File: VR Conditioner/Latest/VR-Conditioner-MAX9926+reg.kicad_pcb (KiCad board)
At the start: 2 copper layers, 19.7 x 19.7 mm, 22 parts, among them J1 8-pin header, J2 Edge, U1 MAX9926UAEE+, U2 AMS1117CD-5.0

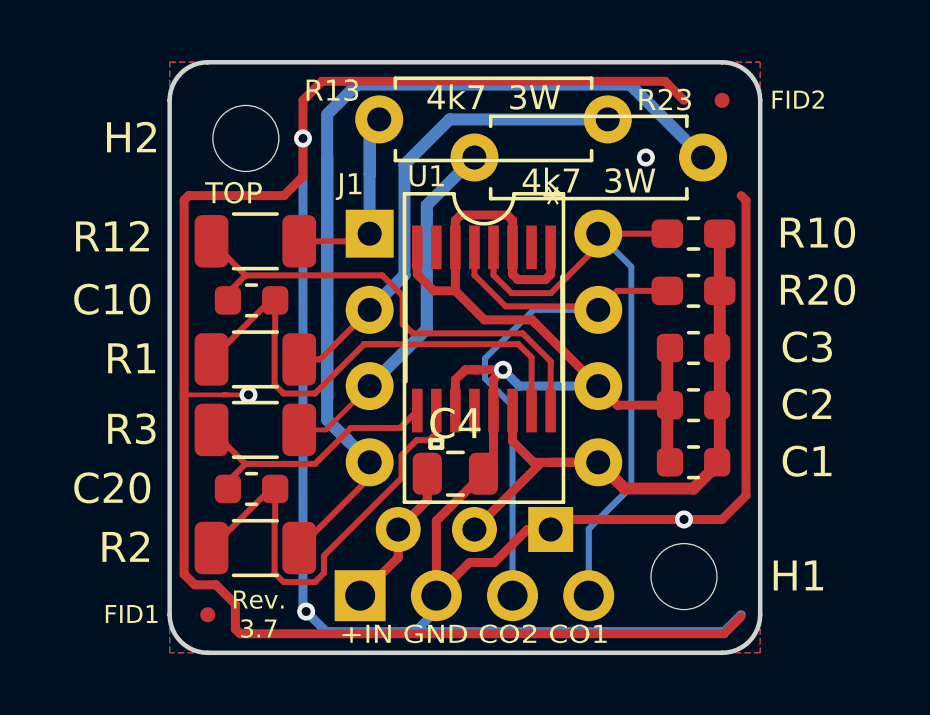
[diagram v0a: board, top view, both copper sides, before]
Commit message: Add prod files for MAX9926 VR cond
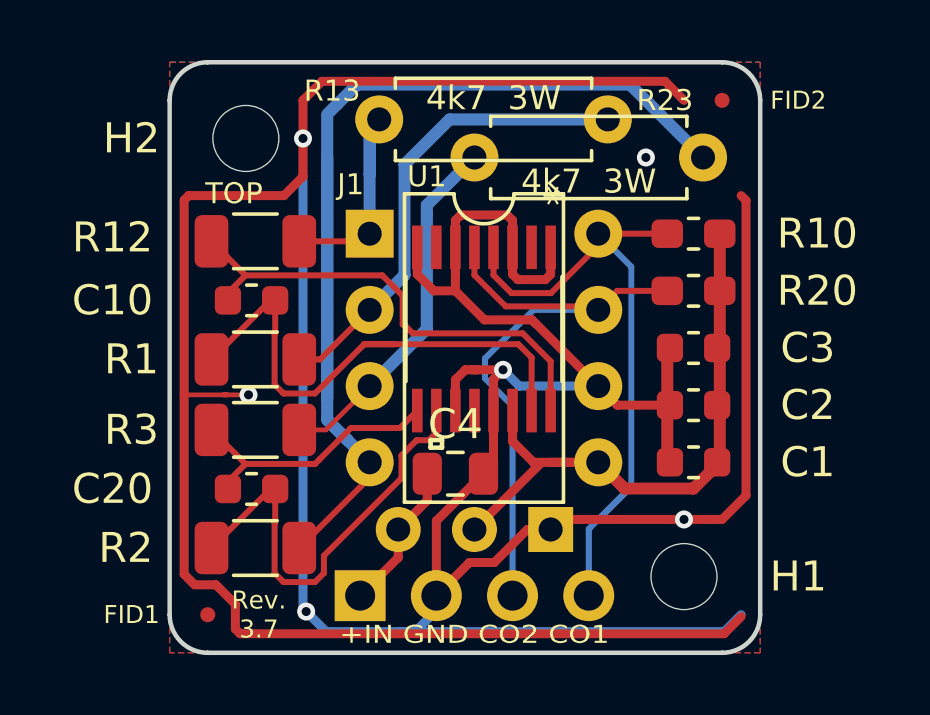
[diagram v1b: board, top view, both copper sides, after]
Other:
- net class Default removed
- net class Minimum removed
- net class power removed
